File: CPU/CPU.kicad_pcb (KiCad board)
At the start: 2 copper layers, 157 x 85.3 mm, 87 parts, among them J101 Conn_02x10_Odd_Even, J102 Conn_02x14_Odd_Even_MountingP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, J301 Conn_02x03_Odd_Even, J302 1X4SMD-FPC, J303 Conn_02x03_Odd_Even, Q101 IRLML0040TR, Q102 IRLML0040TR, Q201 DMC4050, Q301 IRLML0040TR, Q302 IRLML0040TR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

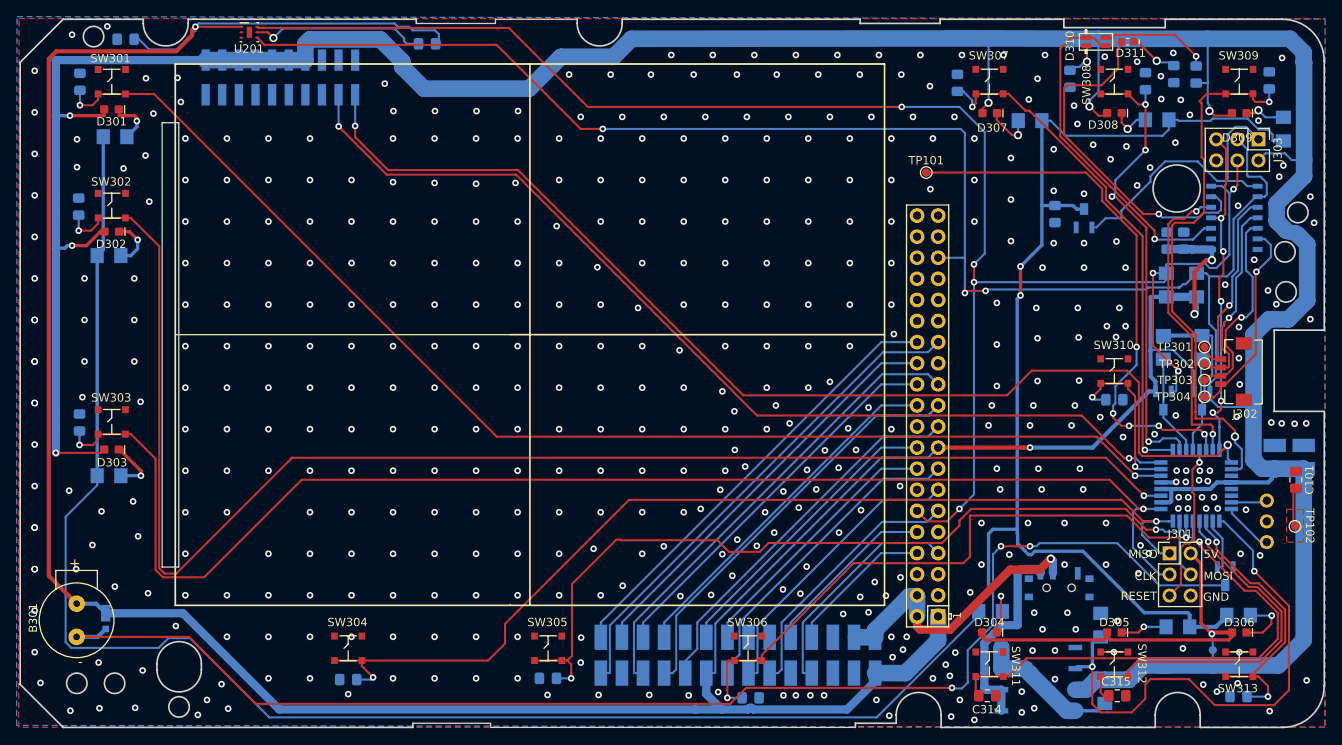
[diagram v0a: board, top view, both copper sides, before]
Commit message: Added the remaining 3D models to the components. Not all are quite accurate but good for visualization. Credit for the RPiWZ 3D model goes to Kevin Schneider at https://gallery.autodesk.com/fusion360/users/200707241731883.
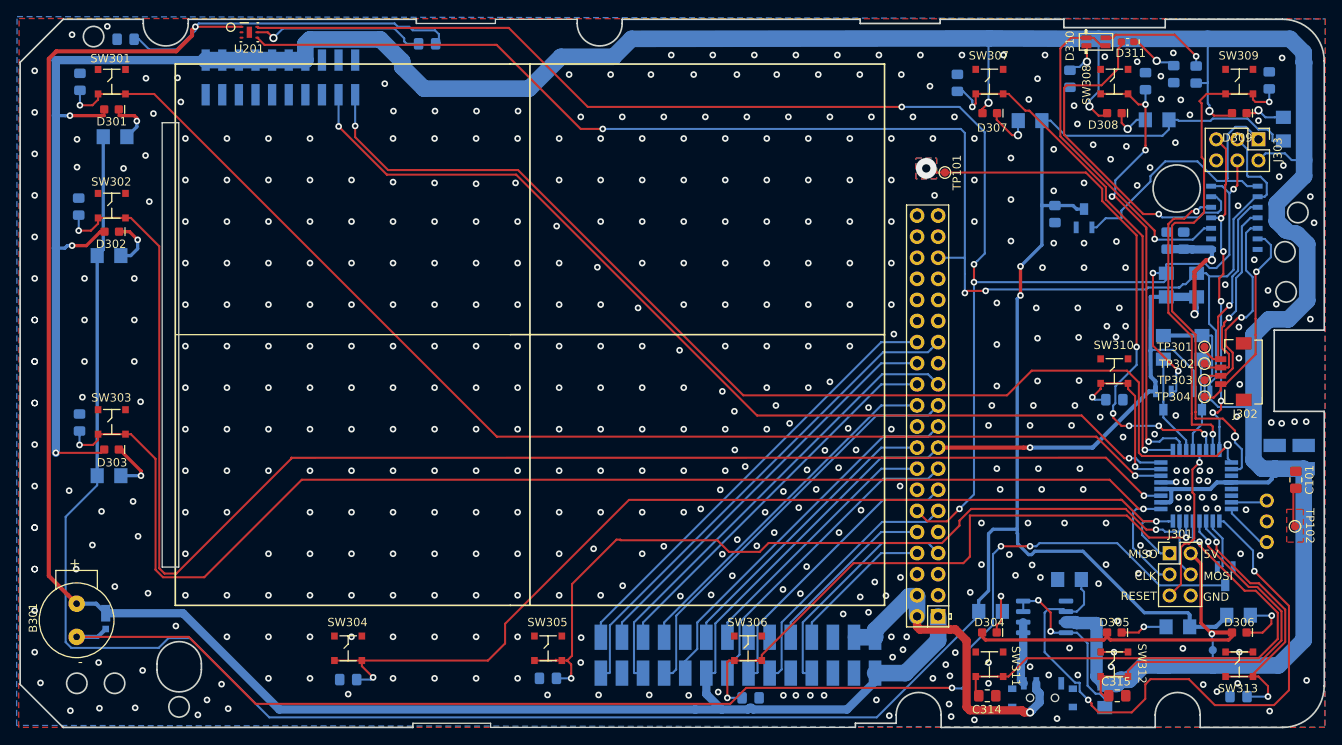
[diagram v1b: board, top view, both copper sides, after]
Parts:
- Q201: footprint Marco:8-SMD -> Package_SO:SO-8_3.9x4.9mm_P1.27mm
- moved SW101 13.4 mm to (153.5, 127.2)
- moved Q201 7.54 mm to (153.8, 117.5), turned to 180 degrees
- moved R209 6.66 mm to (156.8, 113.0), turned to 0 degrees
- moved TP101 2.25 mm to (141.8, 64.0), turned to 270 degrees
- moved R208 0.50 mm to (161.0, 127.0)
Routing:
- net +5VP: track 24.5 -> 7.62 mm
- net /Micro Controller Devices/PI_PWR_SW: track 63.8 -> 75.3 mm
- net 5V: track 468.9 -> 476.5 mm
- net /Pi5V: track 35.2 -> 40.3 mm
- net Net-(Q201-Pad4): track 17.5 -> 21.4 mm, vias 0 -> 2
- net /PI_RESET_TOGGLE: track 66.3 -> 66.8 mm, vias 5 -> 6
- net GND: vias 491 -> 492
- added copper zone on B.Cu, net /PI_RESET_TOGGLE
- added copper zone on F.Cu, net /PI_RESET_TOGGLE
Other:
- board text added: "Pi ~RES~"

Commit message: Before correcting the PCB geometry.
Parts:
- added REF**: MountingHole_2mm, MountingHole:MountingHole_2mm, F.Cu at (100.2, 50.5)
- moved D310 0.31 mm to (160.2, 48.2)
- moved D311 0.25 mm to (164.0, 48.2)

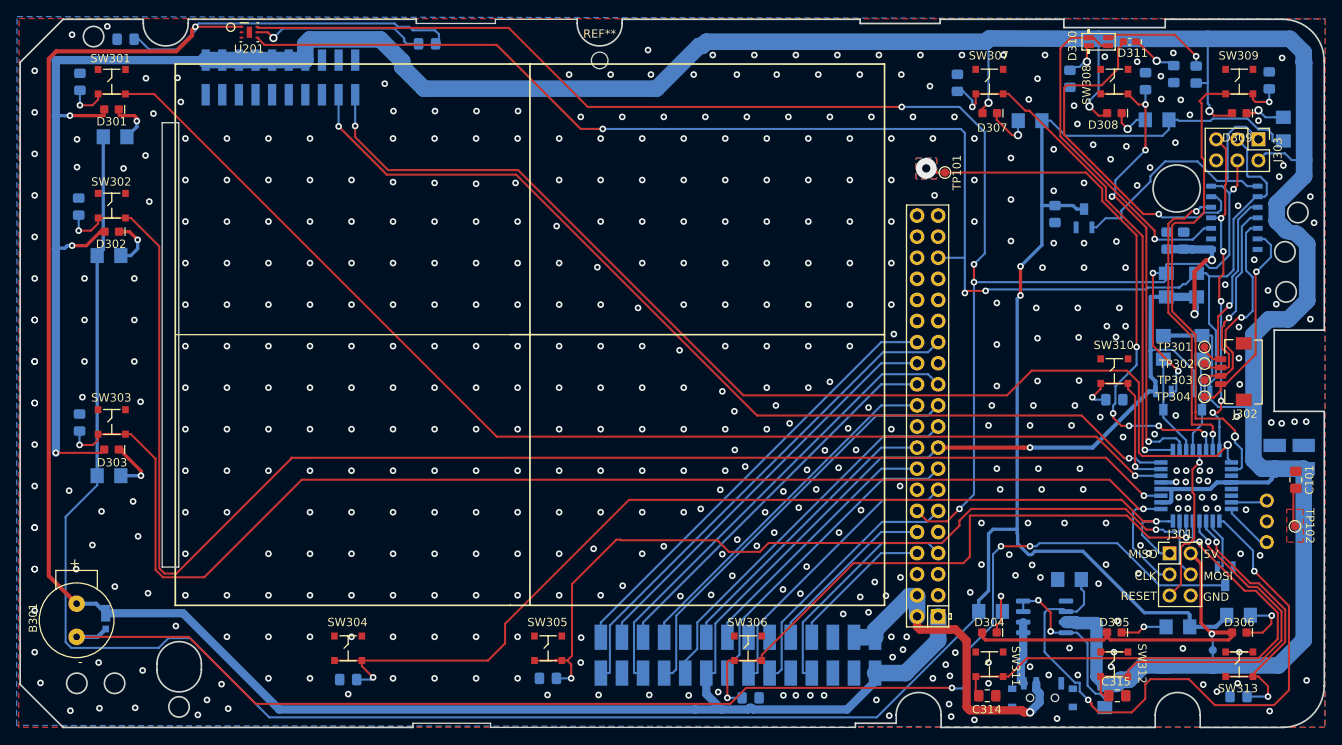
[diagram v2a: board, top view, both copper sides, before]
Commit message: Fixed the PCB outlines so they are at the correct angles.
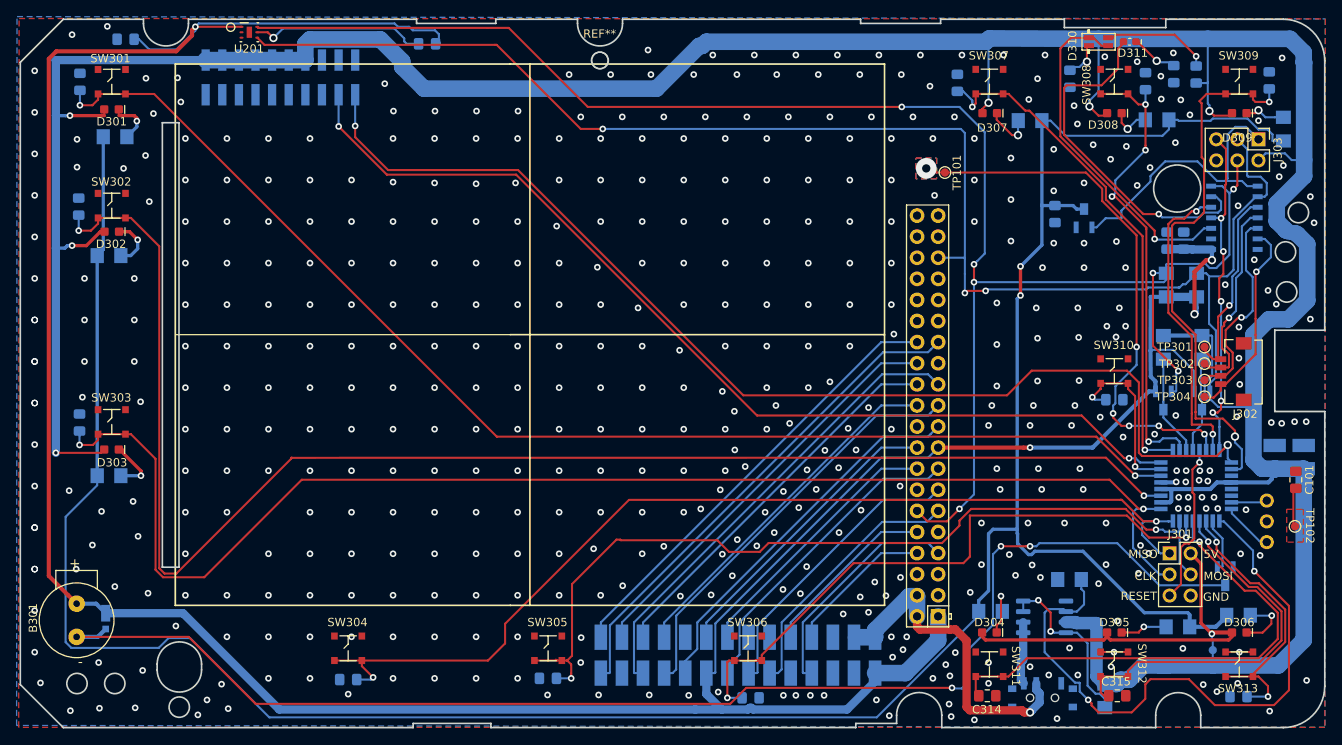
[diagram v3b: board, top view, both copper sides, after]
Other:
- board size 157 x 85.3 mm -> 157.1 x 85.3 mm

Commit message: Corrected the issues with v1 of the CPU board. Moved to 0.8mm board. Should be ready for another order.
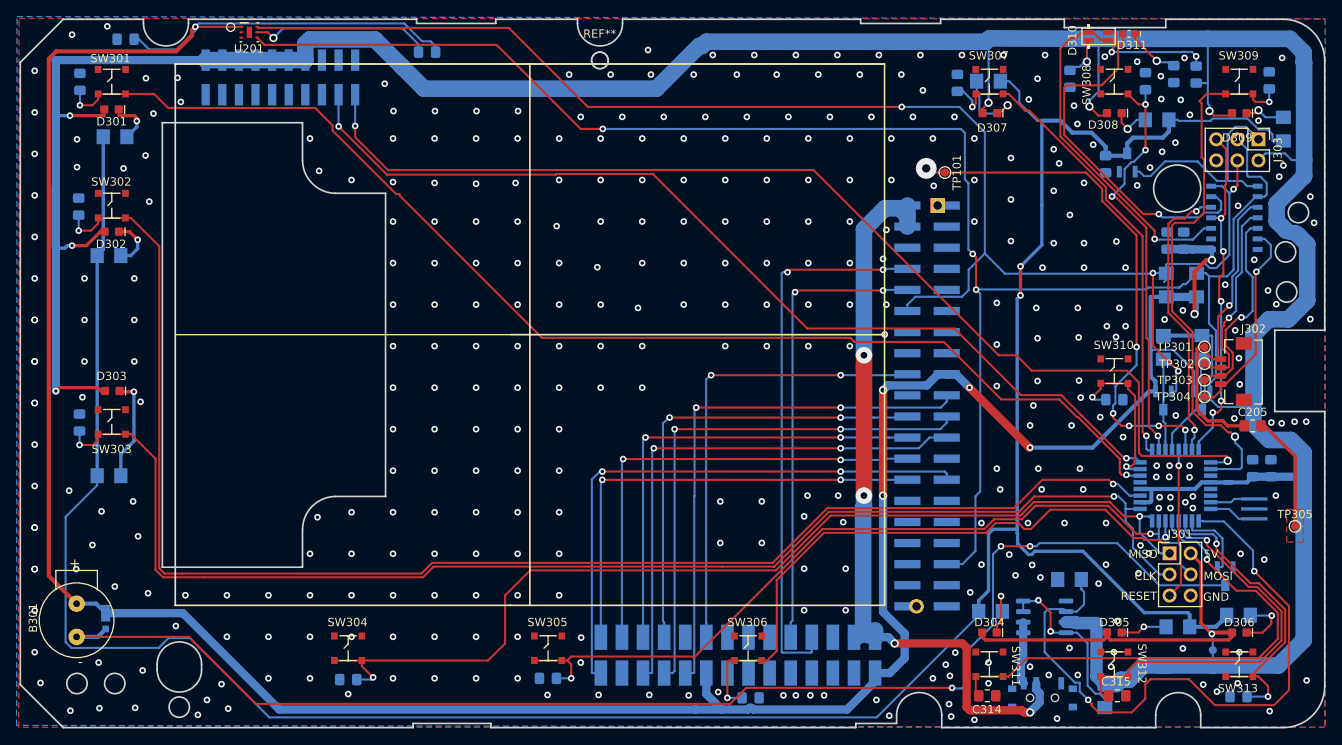
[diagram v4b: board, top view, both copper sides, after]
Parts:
- removed C101: 47uF, Capacitor_SMD:C_0805_2012Metric_Pad1.15x1.40mm_HandSolder
- removed TP102: TestPoint, TestPoint:TestPoint_Pad_D1.0mm
- added C205: 47uF, Capacitor_SMD:C_0805_2012Metric_Pad1.15x1.40mm_HandSolder, F.Cu at (178.8, 94.5)
- added TP305: TestPoint, TestPoint:TestPoint_Pad_D1.0mm, F.Cu at (183.9, 106.6)
- C301, C303: footprint CPU:C1210 -> Capacitor_SMD:C_0805_2012Metric_Pad1.15x1.40mm_HandSolder
- Pi101: footprint CPU:RASPBERRYPI_Zero-No_Mounting_Holes -> CPU:RASPBERRYPI_Zero-No_Mounting_Holes_SMD_Flat; moved to B.Cu
- Y301: footprint Crystal:Resonator-3Pin_W7.0mm_H2.5mm -> Crystal:Resonator_SMD_muRata_CSTxExxV-3Pin_3.0x1.1mm_HandSoldering
- moved Pi101 66.2 mm to (166.1, 59.6), turned to 270 degrees
- moved C204 8.56 mm to (161.1, 63.0)
- moved Q301 8.48 mm to (163.7, 62.8)
- moved D303 7.05 mm to (41.5, 90.3)
- moved R307 6.90 mm to (147.0, 53.0)
- moved C303 4.17 mm to (181.0, 99.6)
- moved C301 2.97 mm to (178.8, 99.6)
- moved U301 2.50 mm to (169.5, 101.7)
- moved Y301 1.80 mm to (179.0, 104.5)
- moved R201 1.00 mm to (79.4, 49.5)
- moved D311 0.96 mm to (163.9, 47.3)
- moved D310 0.65 mm to (160.2, 47.6)
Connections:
- Pi101 pad 1: +3V3 -> Net-(Pi101-Pad1)
- Pi101 pad 11: /Pi11 -> Net-(Pi101-Pad11)
- Pi101 pad 13: /Pi13 -> Net-(Pi101-Pad13)
- Pi101 pad 15: /Pi15 -> Net-(Pi101-Pad15)
- Pi101 pad 16: /Pi16 -> Net-(Pi101-Pad16)
- Pi101 pad 7: /Pi7 -> Net-(Pi101-Pad7)
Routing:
- net /Pi5V: track 40.3 -> 92.0 mm, vias 1 -> 4
- net /UARTA: track 17.9 -> 66.4 mm, vias 0 -> 2
- net /Pi15: track 38.3 -> 0.00 mm
- net /Pi13: track 35.3 -> 0.00 mm
- net /UARTB: track 21.5 -> 55.4 mm, vias 0 -> 2
- net /Pi16: track 32.3 -> 0.00 mm
- net /Pi11: track 31.7 -> 0.00 mm
- net /SCL: track 181.1 -> 212.6 mm
- net /Pi7: track 27.9 -> 0.00 mm
- net /SDA: track 211.1 -> 185.4 mm, vias 7 -> 4
- net /RT_INIT: track 35.9 -> 55.5 mm, vias 0 -> 2
- net /MOSI: track 45.5 -> 64.3 mm, vias 0 -> 2
- net /I2C Devices/SCC: track 23.9 -> 38.7 mm
- net /I2C Devices/TGUARD: track 0.00 -> 14.3 mm
- net /MISO: track 50.1 -> 64.3 mm, vias 0 -> 2
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- added copper zone on F.Cu, net /I2C Devices/TGUARD
- removed copper zone on B.Cu, net /PI_RESET_TOGGLE
- removed copper zone on F.Cu, net /PI_RESET_TOGGLE
- removed copper zone on F.Cu, net /TGUARD
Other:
- outline, holes or cut-outs redrawn

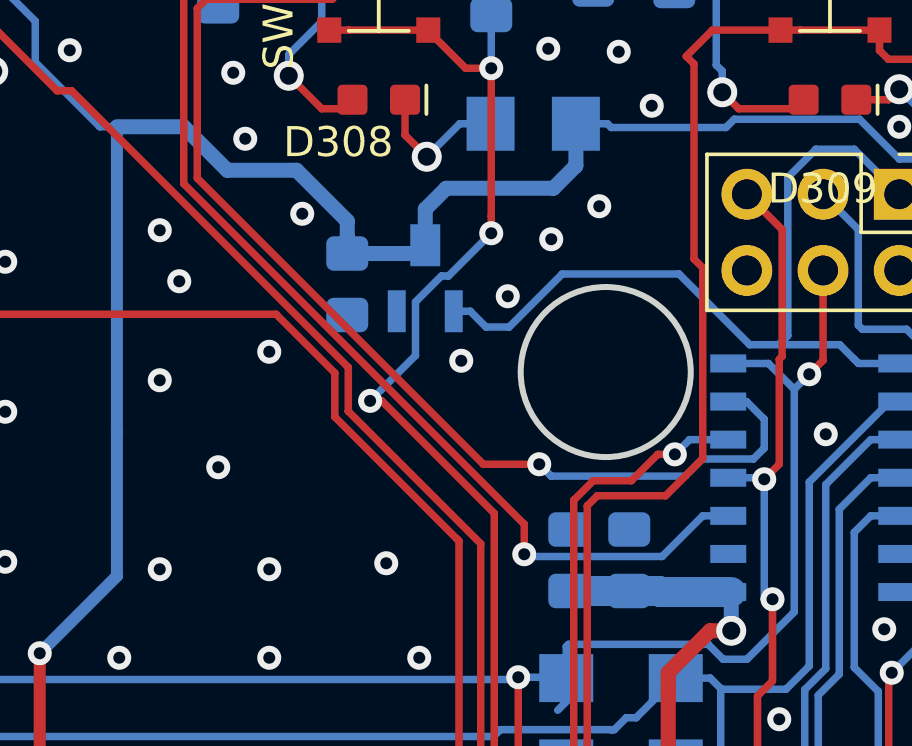
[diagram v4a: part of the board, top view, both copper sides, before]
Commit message: Rewiring the T84 to the 5 volt line.
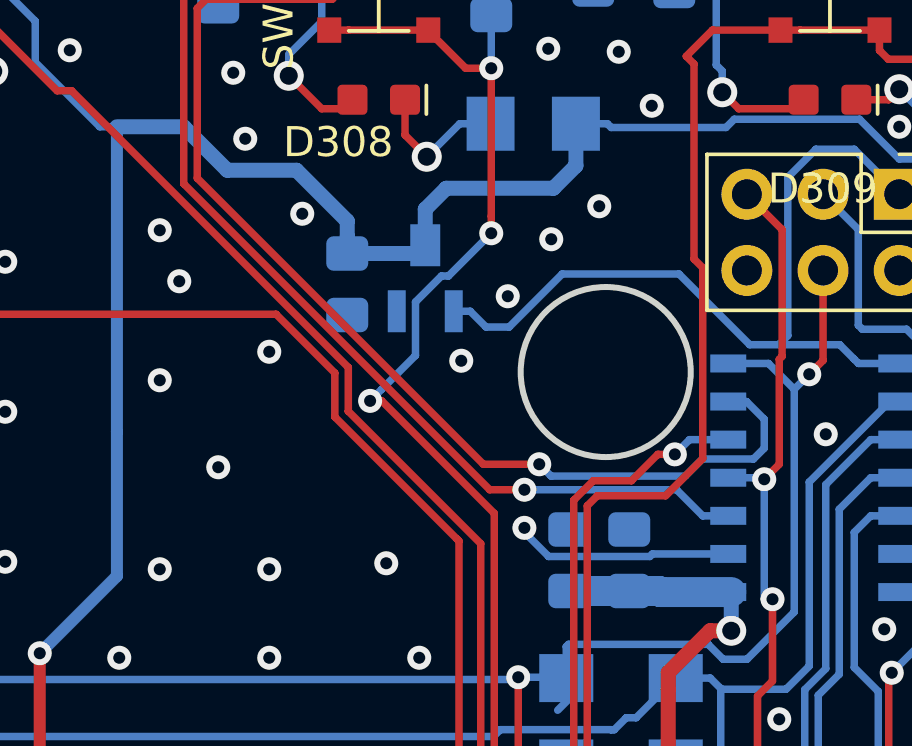
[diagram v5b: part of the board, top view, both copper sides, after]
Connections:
- D310 pad 1: /I2C Devices/R_G -> Net-(D310-Pad1)
- D310 pad 2: Net-(D310-Pad2) -> 5V
- D310 pad 4: /I2C Devices/R_G -> 5V
- D311 pad A: /I2C Devices/ORANGE -> 5V
- R310 pad 1: Net-(D310-Pad2) -> /I2C Devices/GREEN
- R310 pad 2: 5V -> Net-(D310-Pad1)
- R311 pad 2: GND -> /I2C Devices/RED
- R312 pad 2: GND -> /I2C Devices/ORANGE
- U202 pad 2: Net-(U202-Pad2) -> /I2C Devices/GREEN
- U202 pad 3: /I2C Devices/R_G -> /I2C Devices/RED
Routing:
- net /I2C Devices/GREEN: track 0.00 -> 7.31 mm, vias 0 -> 1
- net /I2C Devices/R_G: track 42.0 -> 40.3 mm
